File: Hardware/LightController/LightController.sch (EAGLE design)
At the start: 28 parts, among them IC1 ATMEGA328P, K1 G5LE, Q1 8MHz, Q2 2N3704, X1 IN, X2 OUT, X3 EARTH

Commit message: updated processoor to be surface mount. created intial route for pcb tracks. Had to use dual layer board to allow for small form factor
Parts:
- removed IC1: ATMEGA328P, ic-package:DIL28-3
- added IC2: ATMEGA328P-AU, ATMEGA328P:ATMEGA328P-AU
- LED1, LED2: device led:LED5MM -> led:LEDSMT1206
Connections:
- removed net N$10: IC1.12, R4.2
- new net N$19: IC2.(PCINT21/OC0B/T1)PD5, R3.2
- net +3V3: now also IC2.AREF, IC2.AVCC, IC2.VCC, IC2.VCC@1; no longer IC1.20, IC1.21, IC1.7
- net CE_RAD: now also IC2.(PCINT2/!SS!/OC1B)PB2; no longer IC1.16
- net CSN_RAD: now also IC2.(PCINT1/OC1A)PB1; no longer IC1.15
- net GND: now also IC2.GND, IC2.GND@1, IC2.GND@2; no longer IC1.22, IC1.8
- net MISO: now also IC2.(PCINT4/MISO)PB4; no longer IC1.18
- net MOSI: now also IC2.(PCINT3/OC2A/MOSI)PB3; no longer IC1.17
- net N$1: now also K12.S; no longer K12.P
- net N$13: now also K12.P, X2-2.KL; no longer K12.S, X2-1.KL
- net N$3: now also IC2.(!RESET!/PCINT14)PC6; no longer IC1.1
- net N$4: now also X2-1.KL; no longer X2-2.KL
- net N$5: now also IC2.(PCINT22/OC0A/AIN0)PD6, R4.2; no longer IC1.11, R3.2
- net N$7: now also IC2.(ADC5/SCL/PCINT13)PC5; no longer IC1.28
- net N$8: now also IC2.(PCINT6/XTAL1/TOSC1)PB6; no longer IC1.9
- net N$9: now also IC2.(PCINT7/XTAL2/TOSC)PB7; no longer IC1.10
- net SCK: now also IC2.(SCK/PCINT5)PB5; no longer IC1.19
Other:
- moved on the sheet: K1, L2, L3, LED1, LED2, OK1, Q2, R1, R3, R4, R5, R7

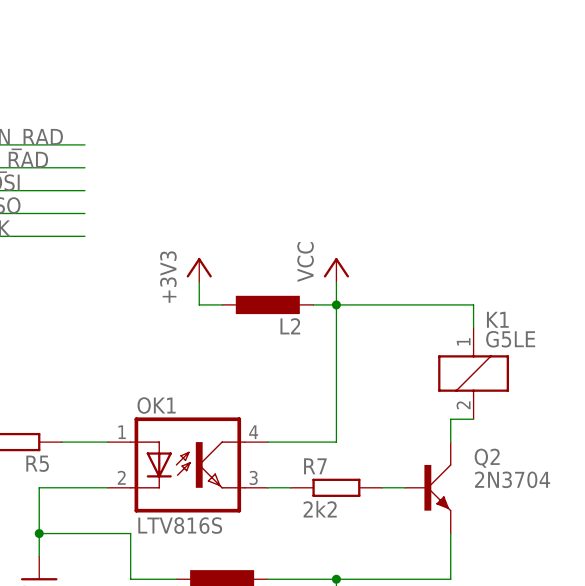
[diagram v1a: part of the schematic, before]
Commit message: added flyback diode and tidied traces
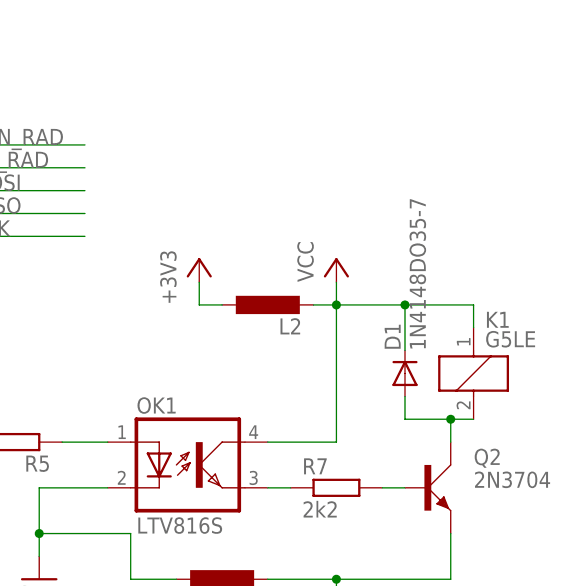
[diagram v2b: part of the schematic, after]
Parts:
- added D1: 1N4148DO35-7, diode:1N4148DO35-7
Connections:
- net N$16: now also D1.A
- net VCC: now also D1.C
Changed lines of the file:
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@@
 <part name="+3V6" library="supply1" deviceset="+3V3" device=""/>
 <part name="GND5" library="supply1" deviceset="GND" device=""/>
+<part name="D1" library="diode" deviceset="1N4148" device="DO35-7"/>
 </parts>
 <sheets>
@@
 <instance part="+3V6" gate="G$1" x="88.9" y="88.9"/>
 <instance part="GND5" gate="1" x="86.36" y="2.54"/>
+<instance part="D1" gate="G$1" x="259.08" y="48.26" rot="R90"/>
 </instances>
 <busses>
@@
 <pinref part="K1" gate="1" pin="1"/>
 <wire x1="266.7" y1="53.34" x2="266.7" y2="55.88" width="0.1524" layer="91"/>
-<wire x1="266.7" y1="55.88" x2="251.46" y2="55.88" width="0.1524" layer="91"/>
+<wire x1="266.7" y1="55.88" x2="259.08" y2="55.88" width="0.1524" layer="91"/>
 <pinref part="OK1" gate="G$1" pin="COL"/>
+<wire x1="259.08" y1="55.88" x2="251.46" y2="55.88" width="0.1524" layer="91"/>
 <wire x1="251.46" y1="40.64" x2="243.84" y2="40.64" width="0.1524" layer="91"/>
 <wire x1="251.46" y1="40.64" x2="251.46" y2="55.88" width="0.1524" layer="91"/>
+<pinref part="D1" gate="G$1" pin="C"/>
+<wire x1="259.08" y1="50.8" x2="259.08" y2="55.88" width="0.1524" layer="91"/>
+<junction x="259.08" y="55.88"/>
 </segment>
 </net>
@@
 <wire x1="264.16" y1="40.64" x2="264.16" y2="43.18" width="0.1524" layer="91"/>
 <wire x1="264.16" y1="43.18" x2="266.7" y2="43.18" width="0.1524" layer="91"/>
-</segment>
-</net>
+<pinref part="D1" gate="G$1" pin="A"/>
+<wire x1="259.08" y1="45.72" x2="259.08" y2="43.18" width="0.1524" layer="91"/>
+<wire x1="259.08" y1="43.18" x2="264.16" y2="43.18" width="0.1524" layer="91"/>
+<junction x="264.16" y="43.18"/>
+</segment>
+</net>
